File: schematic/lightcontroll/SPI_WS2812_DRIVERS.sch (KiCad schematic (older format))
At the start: 18 parts, among them J26 SK2812_sig, J28 Conn_01x03, J9 SPI 5V, U4 74LS123, U5 7402, U6 TXB0104D, U9 7402

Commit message: save Version 1.0
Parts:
- C27, C28, C29, C30: Mouser (none) -> https://www.mouser.de/ProductDetail/Wurth-Elektronik/885012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
- C31, C32: value 200 pF -> 200pF; Mouser (none) -> https://www.mouser.de/ProductDetail/KEMET/C0603C201G1HACTU?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
- D2, D3: Mouser (none) -> https://www.mouser.de/ProductDetail/Comchip-Technology/CDBU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
- U4: Mouser (none) -> https://www.mouser.de/ProductDetail/Texas-Instruments/SN74L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
- U5, U9: Mouser (none) -> https://www.mouser.de/ProductDetail/Texas-Instruments/SN74H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
- U5: Mouser https://www.mouser.de/ProductDetail/Texas-Instruments/SN74HCT02D?qs=sGAEpiMZZMtMa9lbYwD6ZAv0bRAq9ZjLhmhvx7vjjy0%3D -> https://www.mouser.de/ProductDetail/Texas-Instruments/SN74HCT02DR?qs=sGAEpiMZZMtMa9lbYwD6ZJeO7ZVi7W4dXAwvCCwNxTo%3D
- U6: Mouser (none) -> https://www.mouser.de/ProductDetail/Texas-Instruments/TXB01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

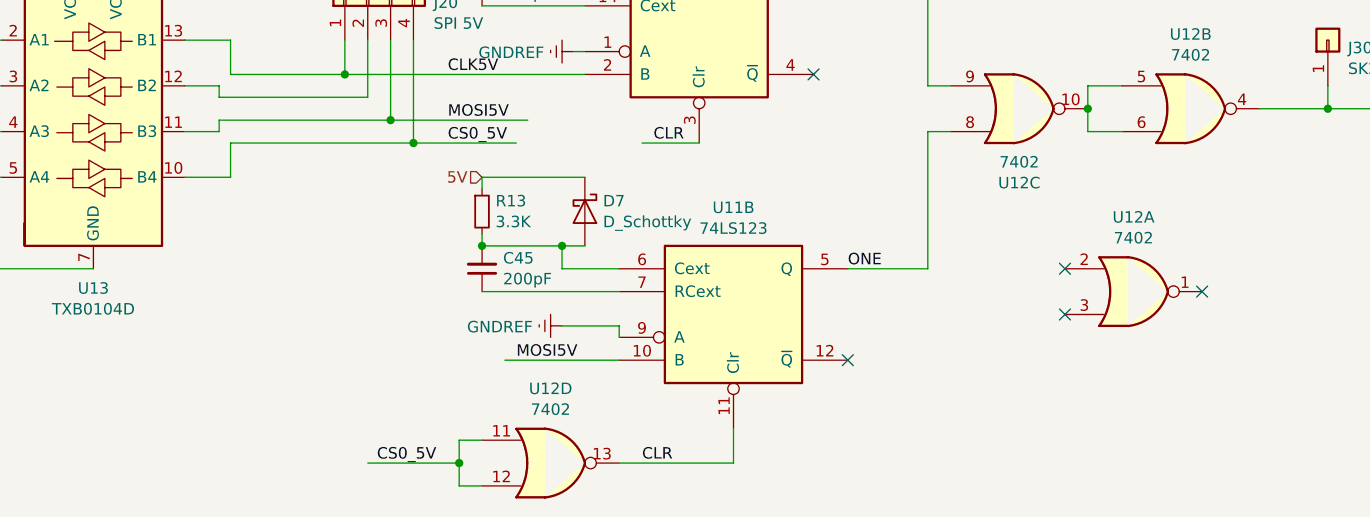
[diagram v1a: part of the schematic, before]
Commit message: Updated PCB to Revision 2.0
- Added an 2.54mm pin header for second RS232 UART, which was already available in rev 1.0
- Changed all 2.00mm pin header to 2.54mm pin header. This fixes the mistake done in selecting the wrong footprint in rev 1.0
- Corrected schematic and layout of the spi to sk2812 circuits. During testing of previous rev some mistakes where found.
	* the second logical schemitac part of 74ls123 changes meaning of pin 6 and 7 compared to 15 and 14 of the first
	* The vibrator for the one signal needs to be also triggered with every rising edge, so use input A instead of binding it to gnd
	* Use the fourth nand to invert clock signal for a input of one vibrator
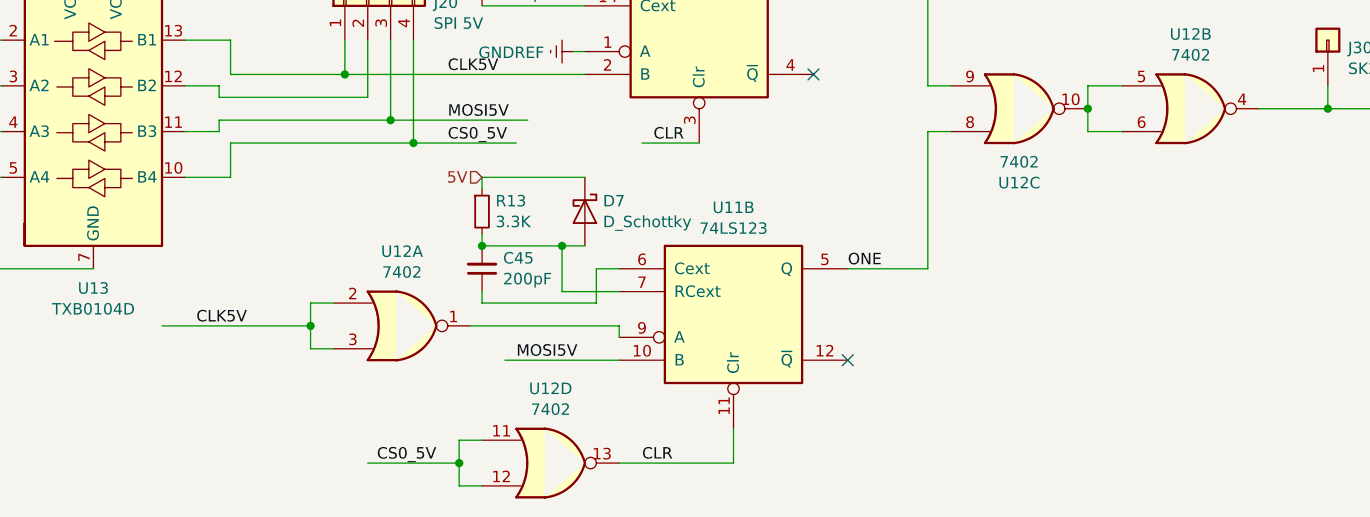
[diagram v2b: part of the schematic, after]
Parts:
- U9: footprint (none) -> Package_SO:SOIC-14_3.9x8.7mm_P1.27mm
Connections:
- wire segments 84 -> 92
- no-connect marks 5 -> 2
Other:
- moved on the sheet: U12A
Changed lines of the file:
@@
 $Descr A4 11693 8268
 encoding utf-8
-Sheet 8 9
+Sheet 7 9
 Title "SPI to WS2812 Circuit"
-Date "2020-05-25"
-Rev "1.1"
+Date "2021-04-10"
+Rev "2.0"
 Comp "Tibersam Industries"
 Comment1 ""
@@
 Wire Wire Line
 	3800 4100 4300 4100
-$Comp
-L power:GNDREF #PWR048
-U 1 1 5CA5DBD4
-P 4050 3950
-AR Path="/5C987024/5CA5DBD4" Ref="#PWR048"  Part="1"
-AR Path="/5EBD8EEE/5CA5DBD4" Ref="#PWR058"  Part="1"
-AR Path="/5EBDAB7A/5CA5DBD4" Ref="#PWR067"  Part="1"
-F 0 "#PWR067" H 4050 3700 50  0001 C CNN
-F 1 "GNDREF" V 4055 3822 50  0000 R CNN
-F 2 "" H 4050 3950 50  0001 C CNN
-F 3 "" H 4050 3950 50  0001 C CNN
-	1    4050 3950
-	0    1    1    0
-$EndComp
-Wire Wire Line
-	4050 3950 4300 3950
 Text HLabel 3700 3300 0    50   Input ~ 0
 5V
@@
 	3700 3550 3700 3600
 Wire Wire Line
-	3700 3800 4300 3800
-Wire Wire Line
-	4300 3700 4050 3700
-Wire Wire Line
-	4050 3700 4050 3600
-Wire Wire Line
 	4050 3600 3700 3600
 Connection ~ 3700 3600
@@
 L 74xx:7402 U5
 U 1 1 5CA62BE7
-P 6550 3800
+P 3350 3950
 AR Path="/5C987024/5CA62BE7" Ref="U5"  Part="1"
 AR Path="/5EBD8EEE/5CA62BE7" Ref="U9"  Part="1"
 AR Path="/5EBDAB7A/5CA62BE7" Ref="U12"  Part="1"
-F 0 "U12" H 6550 4125 50  0000 C CNN
-F 1 "7402" H 6550 4034 50  0000 C CNN
-F 2 "Package_SO:SOIC-14_3.9x8.7mm_P1.27mm" H 6550 3800 50  0001 C CNN
-F 3 "http://www.ti.com/lit/gpn/sn7402" H 6550 3800 50  0001 C CNN
-F 4 "https://www.mouser.de/ProductDetail/Texas-Instruments/SN74HCT02DR?qs=sGAEpiMZZMtMa9lbYwD6ZJeO7ZVi7W4dXAwvCCwNxTo%3D" H 6550 3800 50  0001 C CNN "Mouser"
-	1    6550 3800
+F 0 "U12" H 3350 4275 50  0000 C CNN
+F 1 "7402" H 3350 4184 50  0000 C CNN
+F 2 "Package_SO:SOIC-14_3.9x8.7mm_P1.27mm" H 3350 3950 50  0001 C CNN
+F 3 "http://www.ti.com/lit/gpn/sn7402" H 3350 3950 50  0001 C CNN
+F 4 "https://www.mouser.de/ProductDetail/Texas-Instruments/SN74HCT02DR?qs=sGAEpiMZZMtMa9lbYwD6ZJeO7ZVi7W4dXAwvCCwNxTo%3D" H 3350 3950 50  0001 C CNN "Mouser"
+	1    3350 3950
 	1    0    0    -1
 $EndComp
@@
 F 0 "U12" H 4000 4875 50  0000 C CNN
 F 1 "7402" H 4000 4784 50  0000 C CNN
-F 2 "" H 4000 4550 50  0001 C CNN
+F 2 "Package_SO:SOIC-14_3.9x8.7mm_P1.27mm" H 4000 4550 50  0001 C CNN
 F 3 "http://www.ti.com/lit/gpn/sn7402" H 4000 4550 50  0001 C CNN
 F 4 "https://www.mouser.de/ProductDetail/Texas-Instruments/SN74HCT02DR?qs=sGAEpiMZZMtMa9lbYwD6ZJeO7ZVi7W4dXAwvCCwNxTo%3D" H 4000 4550 50  0001 C CNN "Mouser"
@@
 	1    0    0    -1
 $EndComp
-NoConn ~ 6850 3800
-NoConn ~ 6250 3900
-NoConn ~ 6250 3700
+Wire Wire Line
+	3700 3800 3700 3850
+Wire Wire Line
+	3700 3850 4200 3850
+Wire Wire Line
+	4200 3850 4200 3700
+Wire Wire Line
+	4200 3700 4300 3700
+Wire Wire Line
+	4050 3800 4300 3800
+Wire Wire Line
+	4050 3600 4050 3800
+Wire Wire Line
+	3050 3850 2950 3850
+Wire Wire Line
+	2950 3850 2950 3950
+Wire Wire Line
+	2950 4050 3050 4050
+Wire Wire Line
+	2950 3950 2300 3950
+Connection ~ 2950 3950
+Wire Wire Line
+	2950 3950 2950 4050
+Text Label 2450 3950 0    50   ~ 0
+CLK5V
+Wire Wire Line
+	3650 3950 4300 3950
 $EndSCHEMATC
